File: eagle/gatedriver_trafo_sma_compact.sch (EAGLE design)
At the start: 36 parts, among them K1 G5V-2, X4 BU-SMA-V

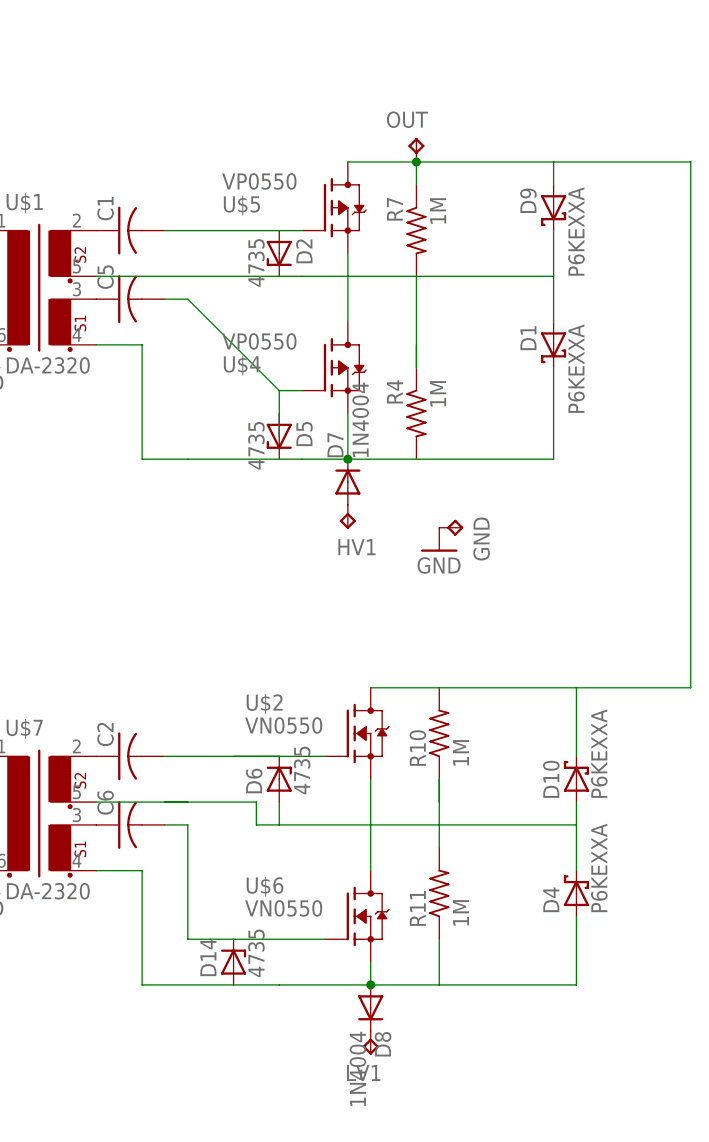
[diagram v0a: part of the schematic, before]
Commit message: darlington gate resistor, diode stacking
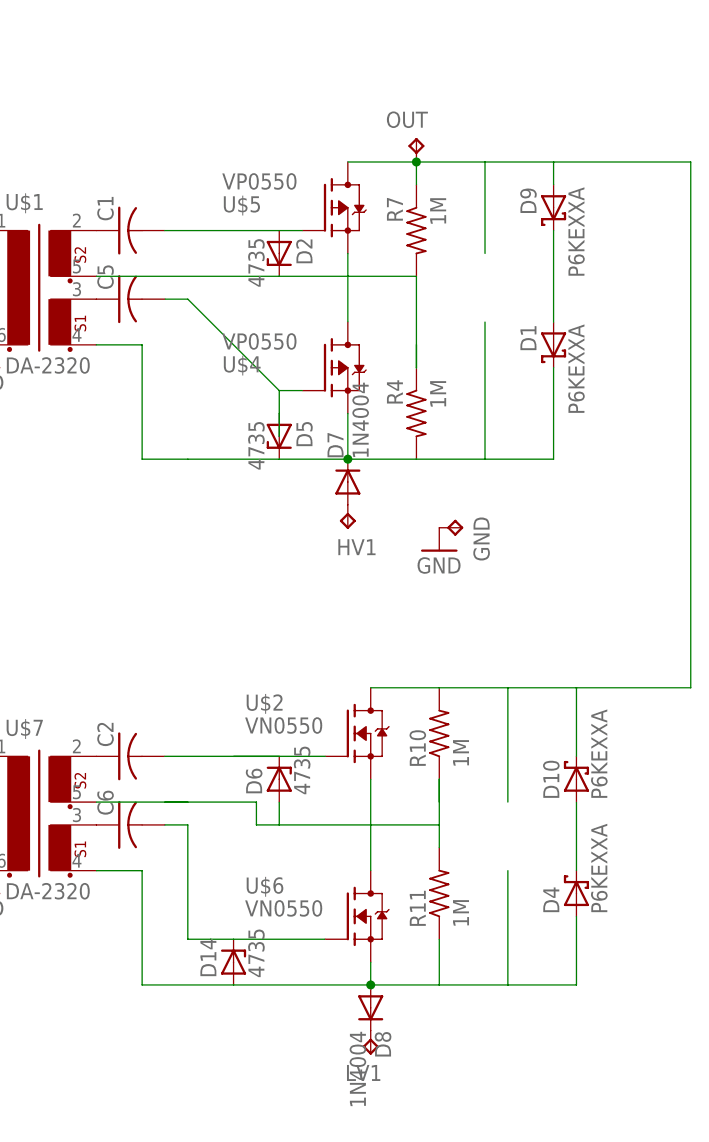
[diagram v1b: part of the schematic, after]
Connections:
- new net N$12: D1.A, D9.C
- new net N$13: D10.A, D4.C
- net N$20: no longer D10.A, D4.C
- net N$21: no longer D1.A, D9.C
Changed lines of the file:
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@@
 <junction x="58.42" y="15.24"/>
 <wire x1="73.66" y1="12.7" x2="73.66" y2="15.24" width="0.1524" layer="91"/>
-<wire x1="73.66" y1="15.24" x2="58.42" y2="15.24" width="0.1524" layer="91"/>
+<wire x1="73.66" y1="15.24" x2="66.04" y2="15.24" width="0.1524" layer="91"/>
 <pinref part="U$5" gate="G$1" pin="D"/>
+<wire x1="66.04" y1="15.24" x2="58.42" y2="15.24" width="0.1524" layer="91"/>
 <wire x1="73.66" y1="15.24" x2="88.9" y2="15.24" width="0.1524" layer="91"/>
 <wire x1="88.9" y1="15.24" x2="88.9" y2="-43.18" width="0.1524" layer="91"/>
@@
 <pinref part="R10" gate="G$1" pin="2"/>
 <wire x1="76.2" y1="-50.8" x2="76.2" y2="-43.18" width="0.1524" layer="91"/>
-<wire x1="76.2" y1="-43.18" x2="60.96" y2="-43.18" width="0.1524" layer="91"/>
+<wire x1="76.2" y1="-43.18" x2="68.58" y2="-43.18" width="0.1524" layer="91"/>
+<wire x1="68.58" y1="-43.18" x2="60.96" y2="-43.18" width="0.1524" layer="91"/>
 <wire x1="60.96" y1="-43.18" x2="53.34" y2="-43.18" width="0.1524" layer="91"/>
 <wire x1="88.9" y1="-43.18" x2="76.2" y2="-43.18" width="0.1524" layer="91"/>
 <pinref part="D9" gate="1" pin="A"/>
 <pinref part="D10" gate="1" pin="C"/>
+<wire x1="66.04" y1="5.08" x2="66.04" y2="15.24" width="0.1524" layer="91"/>
+<wire x1="68.58" y1="-55.88" x2="68.58" y2="-43.18" width="0.1524" layer="91"/>
 </segment>
 </net>
@@
 <pinref part="R4" gate="G$1" pin="2"/>
 <pinref part="D1" gate="1" pin="C"/>
-<wire x1="58.42" y1="-17.78" x2="73.66" y2="-17.78" width="0.1524" layer="91"/>
+<wire x1="58.42" y1="-17.78" x2="66.04" y2="-17.78" width="0.1524" layer="91"/>
+<wire x1="66.04" y1="-17.78" x2="73.66" y2="-17.78" width="0.1524" layer="91"/>
 <wire x1="73.66" y1="-17.78" x2="73.66" y2="-7.62" width="0.1524" layer="91"/>
 <pinref part="U$4" gate="G$1" pin="S"/>
 <wire x1="33.02" y1="-17.78" x2="43.18" y2="-17.78" width="0.1524" layer="91"/>
-<wire x1="45.72" y1="-17.78" x2="50.8" y2="-17.78" width="0.1524" layer="91"/>
+<wire x1="43.18" y1="-17.78" x2="50.8" y2="-17.78" width="0.1524" layer="91"/>
 <wire x1="58.42" y1="-17.78" x2="50.8" y2="-17.78" width="0.1524" layer="91"/>
 <wire x1="50.8" y1="-17.78" x2="50.8" y2="-12.7" width="0.1524" layer="91"/>
@@
 <pinref part="D7" gate="1" pin="C"/>
 <pinref part="D5" gate="G$1" pin="C"/>
-<wire x1="43.18" y1="-17.78" x2="45.72" y2="-17.78" width="0.1524" layer="91"/>
+<wire x1="66.04" y1="-2.54" x2="66.04" y2="-17.78" width="0.1524" layer="91"/>
 </segment>
 </net>
@@
 <wire x1="58.42" y1="2.54" x2="50.8" y2="2.54" width="0.1524" layer="91"/>
 <wire x1="22.86" y1="2.54" x2="43.18" y2="2.54" width="0.1524" layer="91"/>
-<pinref part="D9" gate="1" pin="C"/>
-<pinref part="D1" gate="1" pin="A"/>
-<wire x1="45.72" y1="2.54" x2="50.8" y2="2.54" width="0.1524" layer="91"/>
-<wire x1="73.66" y1="-2.54" x2="73.66" y2="2.54" width="0.1524" layer="91"/>
-<wire x1="73.66" y1="2.54" x2="73.66" y2="7.62" width="0.1524" layer="91"/>
-<wire x1="58.42" y1="2.54" x2="73.66" y2="2.54" width="0.1524" layer="91"/>
+<wire x1="43.18" y1="2.54" x2="50.8" y2="2.54" width="0.1524" layer="91"/>
 <pinref part="D2" gate="G$1" pin="C"/>
-<wire x1="43.18" y1="2.54" x2="45.72" y2="2.54" width="0.1524" layer="91"/>
 </segment>
 </net>
@@
 <pinref part="U$6" gate="G$1" pin="D"/>
 <wire x1="53.34" y1="-63.5" x2="53.34" y2="-58.42" width="0.1524" layer="91"/>
-<pinref part="D10" gate="1" pin="A"/>
-<pinref part="D4" gate="1" pin="C"/>
-<wire x1="76.2" y1="-63.5" x2="76.2" y2="-58.42" width="0.1524" layer="91"/>
-<wire x1="76.2" y1="-58.42" x2="76.2" y2="-55.88" width="0.1524" layer="91"/>
 <pinref part="R11" gate="G$1" pin="2"/>
 <pinref part="R10" gate="G$1" pin="1"/>
@@
 <wire x1="60.96" y1="-53.34" x2="60.96" y2="-58.42" width="0.1524" layer="91"/>
 <wire x1="60.96" y1="-58.42" x2="60.96" y2="-60.96" width="0.1524" layer="91"/>
-<wire x1="60.96" y1="-58.42" x2="76.2" y2="-58.42" width="0.1524" layer="91"/>
 <wire x1="60.96" y1="-58.42" x2="53.34" y2="-58.42" width="0.1524" layer="91"/>
 <wire x1="53.34" y1="-58.42" x2="43.18" y2="-58.42" width="0.1524" layer="91"/>
@@
 <segment>
 <pinref part="D14" gate="G$1" pin="A"/>
-<wire x1="43.18" y1="-76.2" x2="38.1" y2="-76.2" width="0.1524" layer="91"/>
 <pinref part="R11" gate="G$1" pin="1"/>
 <wire x1="60.96" y1="-71.12" x2="60.96" y2="-76.2" width="0.1524" layer="91"/>
 <pinref part="D4" gate="1" pin="A"/>
-<wire x1="60.96" y1="-76.2" x2="76.2" y2="-76.2" width="0.1524" layer="91"/>
+<wire x1="60.96" y1="-76.2" x2="68.58" y2="-76.2" width="0.1524" layer="91"/>
+<wire x1="68.58" y1="-76.2" x2="76.2" y2="-76.2" width="0.1524" layer="91"/>
 <wire x1="76.2" y1="-76.2" x2="76.2" y2="-68.58" width="0.1524" layer="91"/>
 <pinref part="U$7" gate="G$1" pin="3"/>
@@
 <wire x1="27.94" y1="-76.2" x2="38.1" y2="-76.2" width="0.1524" layer="91"/>
 <pinref part="U$6" gate="G$1" pin="S"/>
-<wire x1="43.18" y1="-76.2" x2="53.34" y2="-76.2" width="0.1524" layer="91"/>
+<wire x1="38.1" y1="-76.2" x2="53.34" y2="-76.2" width="0.1524" layer="91"/>
 <wire x1="53.34" y1="-73.66" x2="53.34" y2="-76.2" width="0.1524" layer="91"/>
 <wire x1="60.96" y1="-76.2" x2="53.34" y2="-76.2" width="0.1524" layer="91"/>
 <junction x="53.34" y="-76.2"/>
 <pinref part="D8" gate="1" pin="A"/>
+<wire x1="68.58" y1="-63.5" x2="68.58" y2="-76.2" width="0.1524" layer="91"/>
 </segment>
 </net>
+<net name="N$12" class="0">
+<segment>
+<pinref part="D9" gate="1" pin="C"/>
+<pinref part="D1" gate="1" pin="A"/>
+<wire x1="73.66" y1="-2.54" x2="73.66" y2="7.62" width="0.1524" layer="91"/>
+</segment>
+</net>
+<net name="N$13" class="0">
+<segment>
+<pinref part="D10" gate="1" pin="A"/>
+<pinref part="D4" gate="1" pin="C"/>
+<wire x1="76.2" y1="-63.5" x2="76.2" y2="-55.88" width="0.1524" layer="91"/>
+</segment>
+</net>
